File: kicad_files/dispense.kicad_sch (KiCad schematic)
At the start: 0 parts

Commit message: UI, washout detection, motor schematics finished
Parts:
- added D1, D2: 1N4001, Diode_THT:D_DO-41_SOD81_P10.16mm_Horizontal, symbol Diode:1N4001
- added Q4, Q5: NMOS, symbol Simulation_SPICE:NMOS
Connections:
- new net 5V: Q4.1 (D), Q5.1 (D)
- new net MCU Motor 1: Q4.2 (G)
- new net MCU Motor 2: Q5.2 (G)
- new net Motor Out 1: D1.2 (A), Q4.3 (S)
- new net Motor Out 2: D2.2 (A), Q5.3 (S)
- new net gnd: D1.1 (K), D2.1 (K)

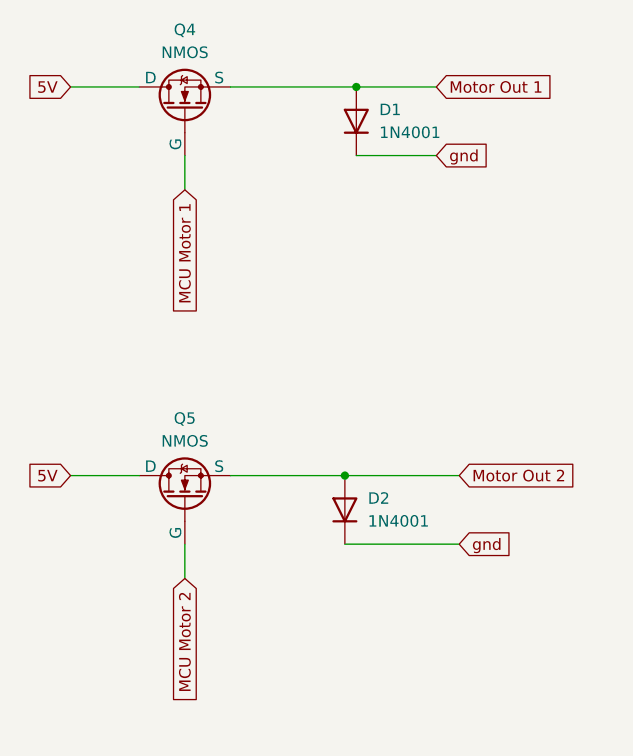
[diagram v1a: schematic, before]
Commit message: Hierarchical labels finished. Flyback diode issue fixed. I2C pins added
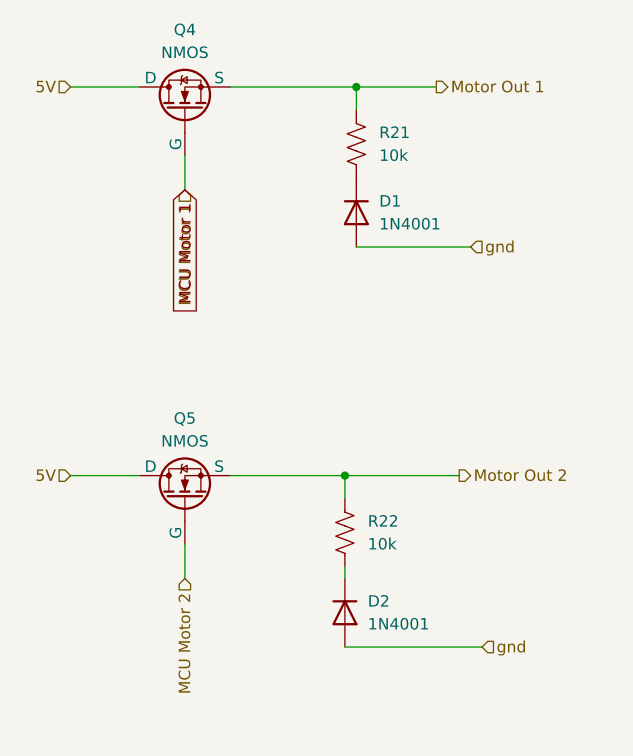
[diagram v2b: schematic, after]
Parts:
- added R21, R22: 10k, symbol Device:R_US
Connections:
- net Motor Out 1: now also R21.1; no longer D1.2 (A)
- net Motor Out 2: now also R22.1; no longer D2.2 (A)
- net gnd: now also D1.2 (A), D2.2 (A); no longer D1.1 (K), D2.1 (K)
- new net: D2.1 (K), R22.2
- new net: D1.1 (K), R21.2
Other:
- moved on the sheet: D1, D2

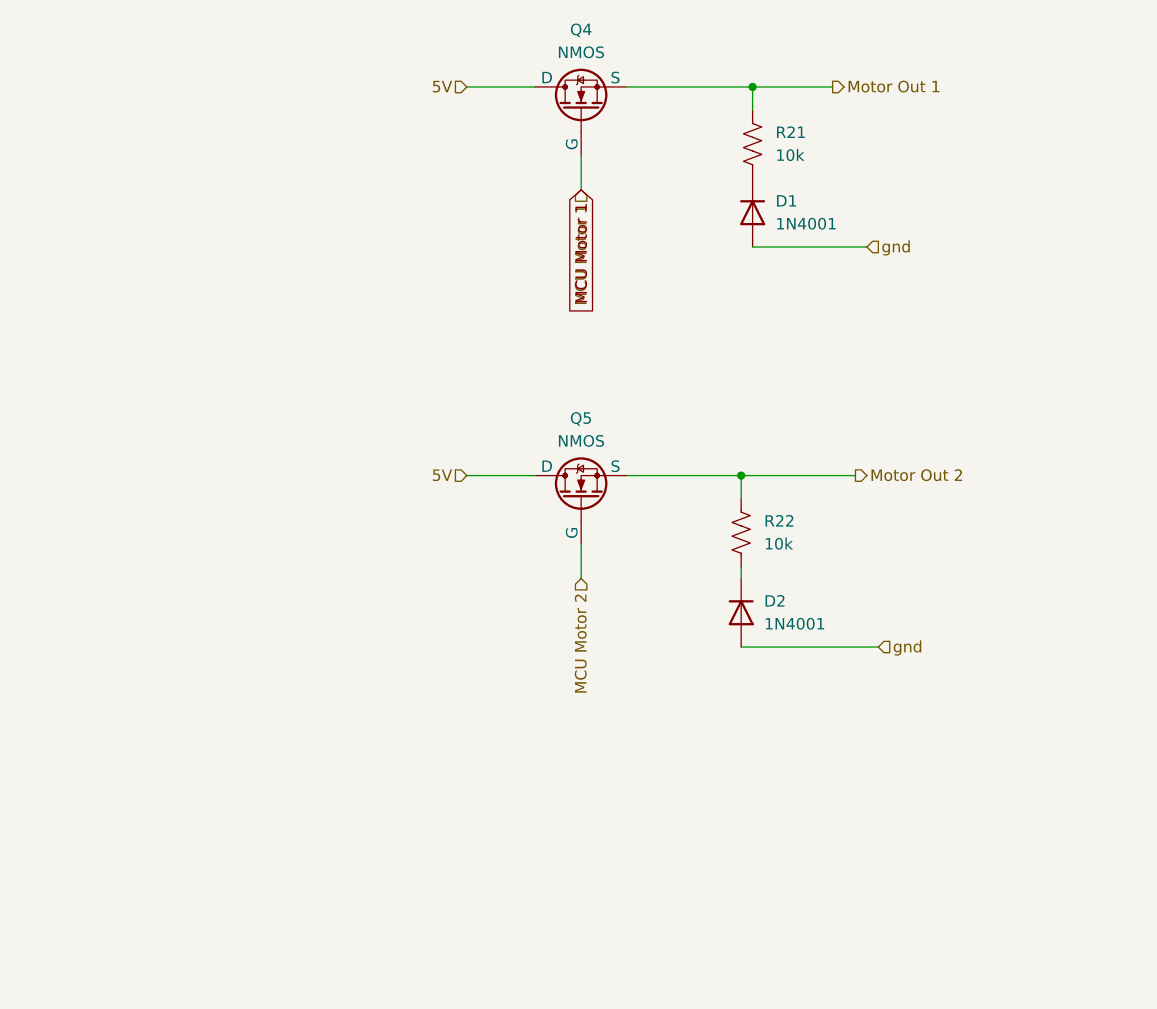
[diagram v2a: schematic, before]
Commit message: ERC errors cleaned. Hierarchical wiring finished. PWM converter change. Motor driver change.
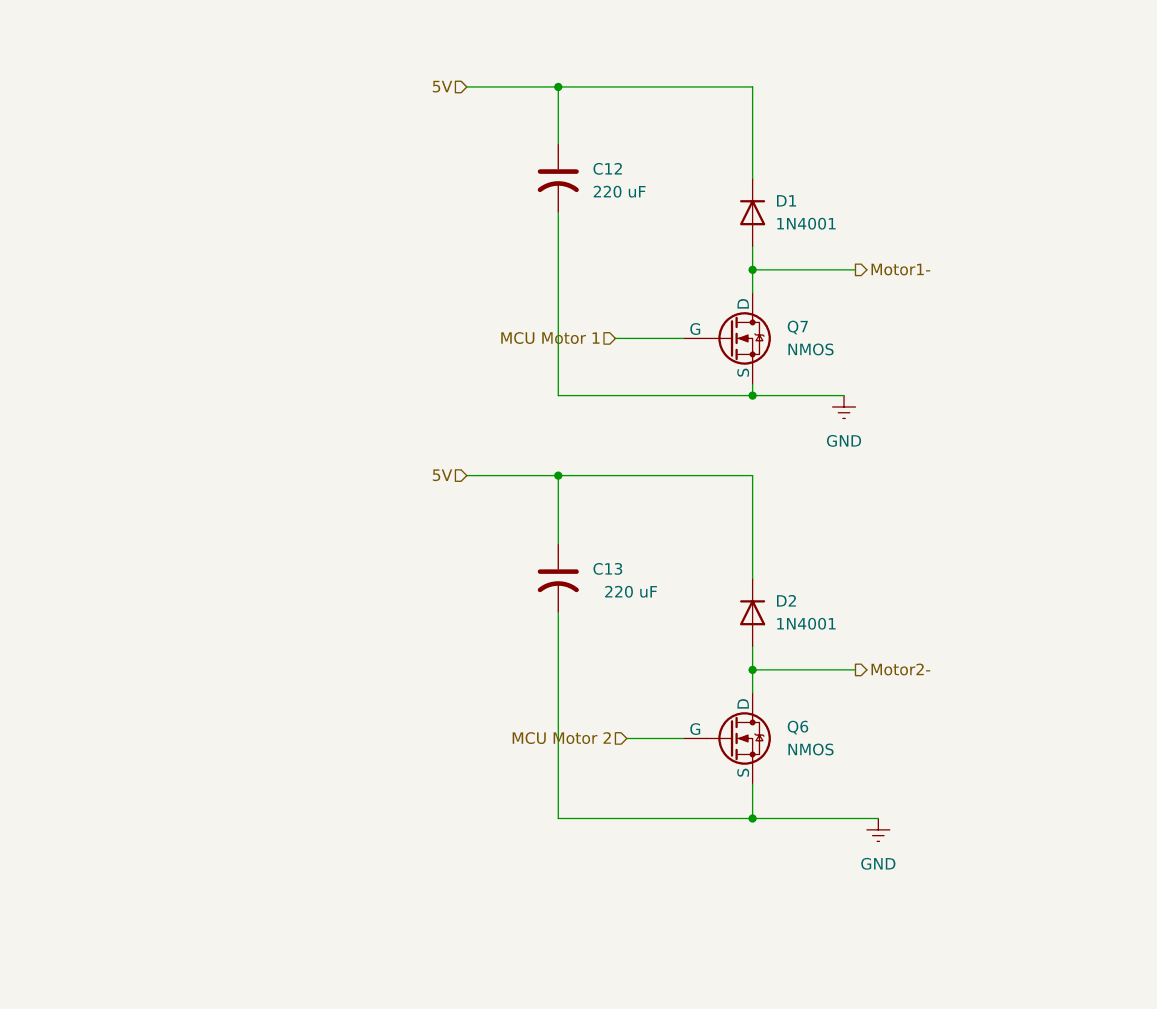
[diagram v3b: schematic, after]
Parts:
- removed Q4, Q5: NMOS, symbol Simulation_SPICE:NMOS
- removed R21, R22: 10k, symbol Device:R_US
- added C12, C13: 220 uF, symbol Device:C_US
- added Q6, Q7: NMOS, symbol Simulation_SPICE:NMOS
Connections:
- net 5V: now also D1.1 (K), D2.1 (K), C12.1, C13.1
- net MCU Motor 1: now also Q7.2 (G)
- net MCU Motor 2: now also Q6.2 (G)
- net gnd renamed Motor1-
- net Motor1-: now also Q7.1 (D); no longer D2.2 (A)
- new net GND: C12.2, C13.2, Q6.3 (S), Q7.3 (S)
- new net Motor2-: D2.2 (A), Q6.1 (D)
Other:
- moved on the sheet: D2

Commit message: minor changes
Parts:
- removed C13: 220 uF, symbol Device:C_US
- removed D2: 1N4001, Diode_THT:D_DO-41_SOD81_P10.16mm_Horizontal, symbol Diode:1N4001
- removed Q6: NMOS, symbol Simulation_SPICE:NMOS
- added Q4, Q5: NMOS, symbol Simulation_SPICE:NMOS
- added R21: 1k, symbol Device:R_US
- added R22, R30: 10k, symbol Device:R_US
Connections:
- net 5V: now also R22.1, R30.1
- net GND: now also Q4.3 (S), Q5.3 (S)
- new net: Q4.1 (D), Q5.2 (G), R22.2
- new net: Q4.2 (G), R21.1
- new net 5V PWM Dispense: Q5.1 (D), R30.2
- new net MCU PWM Dispense: R21.2

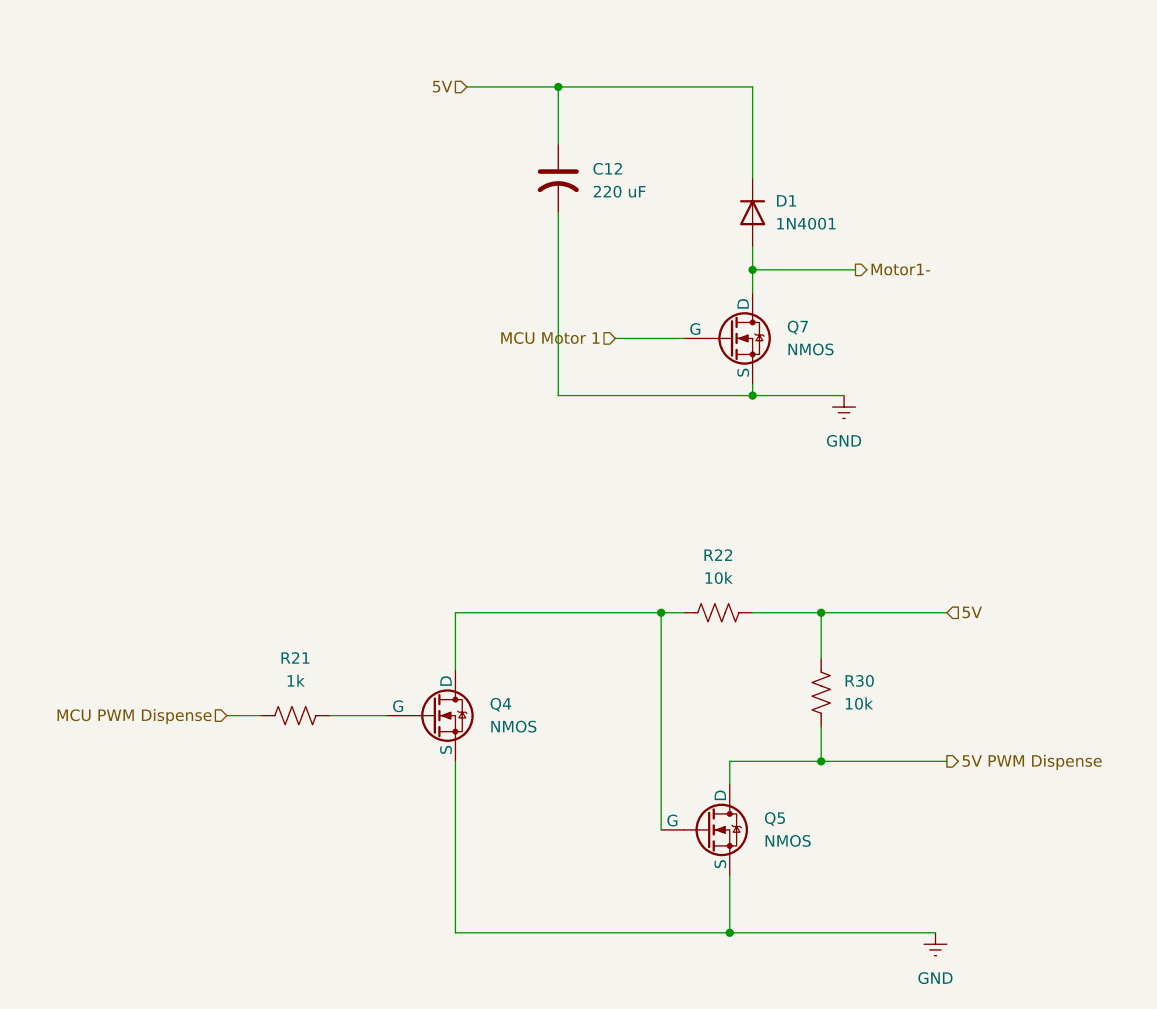
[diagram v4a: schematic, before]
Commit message: Footprint assignment finished
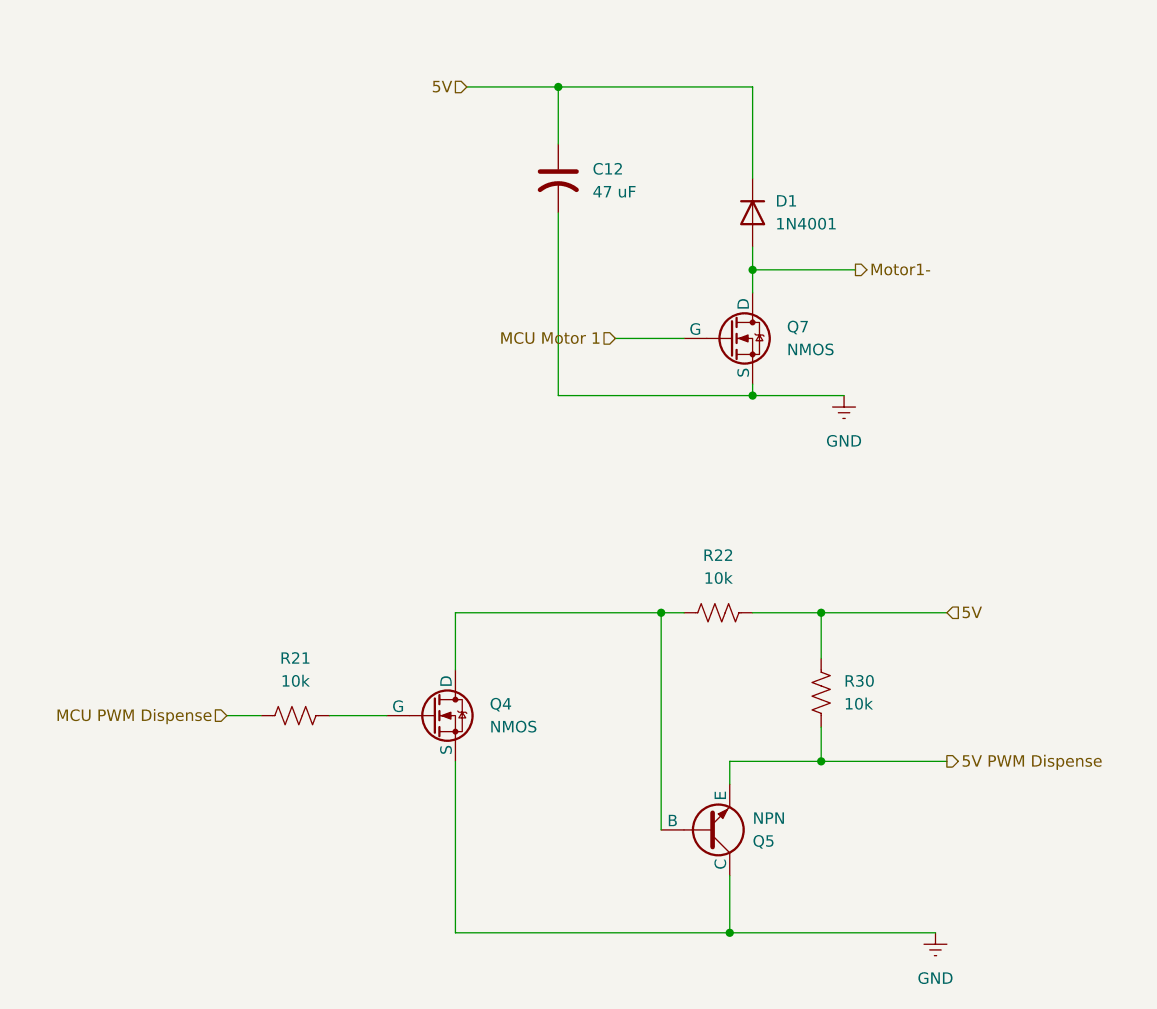
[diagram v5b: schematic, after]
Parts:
- C12: value 220 uF -> 47 uF; footprint (none) -> Capacitor_THT:CP_Radial_D5.0mm_P2.00mm
- Q4: footprint (none) -> Package_TO_SOT_SMD:SOT-323_SC-70
- Q5: value NMOS -> NPN; footprint (none) -> Package_TO_SOT_SMD:TSOT-23; symbol Simulation_SPICE:NMOS -> Simulation_SPICE:NPN
- Q7: footprint (none) -> Package_TO_SOT_SMD:SOT-23-3
- R21: value 1k -> 10k; footprint (none) -> Resistor_SMD:R_1206_3216Metric_Pad1.30x1.75mm_HandSolder
- R22, R30: footprint (none) -> Resistor_SMD:R_1206_3216Metric_Pad1.30x1.75mm_HandSolder
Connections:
- net 5V PWM Dispense: now also Q5.3 (E); no longer Q5.1 (D)
- net GND: now also Q5.1 (C); no longer Q5.3 (S)
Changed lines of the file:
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@@
 			)
 		)
-		(property "Footprint" ""
+		(property "Footprint" "Resistor_SMD:R_1206_3216Metric_Pad1.30x1.75mm_HandSolder"
 			(at 173.736 114.554 90)
 			(effects
@@
 	)
 	(symbol
-		(lib_id "Simulation_SPICE:NMOS")
+		(lib_id "Simulation_SPICE:NPN")
 		(at 160.02 129.54 0)
-		(unit 1)
-		(exclude_from_sim no)
-		(in_bom yes)
-		(on_board yes)
-		(dnp no)
-		(fields_autoplaced yes)
+		(mirror x)
+		(unit 1)
+		(exclude_from_sim no)
+		(in_bom yes)
+		(on_board yes)
+		(dnp no)
 		(property "Reference" "Q5"
-			(at 166.37 128.2699 0)
-			(effects
-				(font
-					(size 1.27 1.27)
-				)
-				(justify left)
-			)
-		)
-		(property "Value" "NMOS"
-			(at 166.37 130.8099 0)
-			(effects
-				(font
-					(size 1.27 1.27)
-				)
-				(justify left)
-			)
-		)
-		(property "Footprint" ""
-			(at 165.1 127 0)
-			(effects
-				(font
-					(size 1.27 1.27)
-				)
-				(hide yes)
-			)
-		)
-		(property "Datasheet" "https://ngspice.sourceforge.io/docs/ngspice-html-manual/manual.xhtml#cha_MOSFETs"
-			(at 160.02 142.24 0)
-			(effects
-				(font
-					(size 1.27 1.27)
-				)
-				(hide yes)
-			)
-		)
-		(property "Description" "N-MOSFET transistor, drain/source/gate"
+			(at 165.1 130.8101 0)
+			(effects
+				(font
+					(size 1.27 1.27)
+				)
+				(justify left)
+			)
+		)
+		(property "Value" "NPN"
+			(at 165.1 128.2701 0)
+			(effects
+				(font
+					(size 1.27 1.27)
+				)
+				(justify left)
+			)
+		)
+		(property "Footprint" "Package_TO_SOT_SMD:TSOT-23"
+			(at 223.52 129.54 0)
+			(effects
+				(font
+					(size 1.27 1.27)
+				)
+				(hide yes)
+			)
+		)
+		(property "Datasheet" "https://ngspice.sourceforge.io/docs/ngspice-html-manual/manual.xhtml#cha_BJTs"
+			(at 223.52 129.54 0)
+			(effects
+				(font
+					(size 1.27 1.27)
+				)
+				(hide yes)
+			)
+		)
+		(property "Description" "Bipolar transistor symbol for simulation only, substrate tied to the emitter"
 			(at 160.02 129.54 0)
 			(effects
@@
 			)
 		)
-		(property "Sim.Device" "NMOS"
-			(at 160.02 146.685 0)
-			(effects
-				(font
-					(size 1.27 1.27)
-				)
-				(hide yes)
-			)
-		)
-		(property "Sim.Type" "VDMOS"
-			(at 160.02 148.59 0)
-			(effects
-				(font
-					(size 1.27 1.27)
-				)
-				(hide yes)
-			)
-		)
-		(property "Sim.Pins" "1=D 2=G 3=S"
-			(at 160.02 144.78 0)
+		(property "Sim.Device" "NPN"
+			(at 160.02 129.54 0)
+			(effects
+				(font
+					(size 1.27 1.27)
+				)
+				(hide yes)
+			)
+		)
+		(property "Sim.Type" "GUMMELPOON"
+			(at 160.02 129.54 0)
+			(effects
+				(font
+					(size 1.27 1.27)
+				)
+				(hide yes)
+			)
+		)
+		(property "Sim.Pins" "1=C 2=B 3=E"
+			(at 160.02 129.54 0)
 			(effects
 				(font
@@
 			)
 		)
-		(property "Value" "1k"
+		(property "Value" "10k"
 			(at 114.3 113.03 90)
 			(effects
@@
 			)
 		)
-		(property "Footprint" ""
+		(property "Footprint" "Resistor_SMD:R_1206_3216Metric_Pad1.30x1.75mm_HandSolder"
 			(at 114.046 117.856 90)
 			(effects
@@
 			)
 		)
-		(property "Footprint" ""
+		(property "Footprint" "Resistor_SMD:R_1206_3216Metric_Pad1.30x1.75mm_HandSolder"
 			(at 161.036 106.426 90)
 			(effects
@@
 			)
 		)
-		(property "Footprint" ""
+		(property "Footprint" "Package_TO_SOT_SMD:SOT-323_SC-70"
 			(at 134.62 114.3 0)
 			(effects
@@
 			)
 		)
-		(property "Footprint" ""
+		(property "Footprint" "Package_TO_SOT_SMD:SOT-23-3"
 			(at 167.64 72.39 0)
 			(effects
@@
 			)
 		)
-		(property "Value" "220 uF"
+		(property "Value" "47 uF"
 			(at 147.32 58.6739 0)
 			(effects
@@
 			)
 		)
-		(property "Footprint" ""
+		(property "Footprint" "Capacitor_THT:CP_Radial_D5.0mm_P2.00mm"
 			(at 143.51 57.15 0)
 			(effects
